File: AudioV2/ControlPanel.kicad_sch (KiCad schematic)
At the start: 39 parts, among them SW1 PWR SW, SW2 DEST sense (3PDT 3rd pole), U1 Pico 2 / RP2350, U2 PT2314-D, U5 BP5293-50 +5V

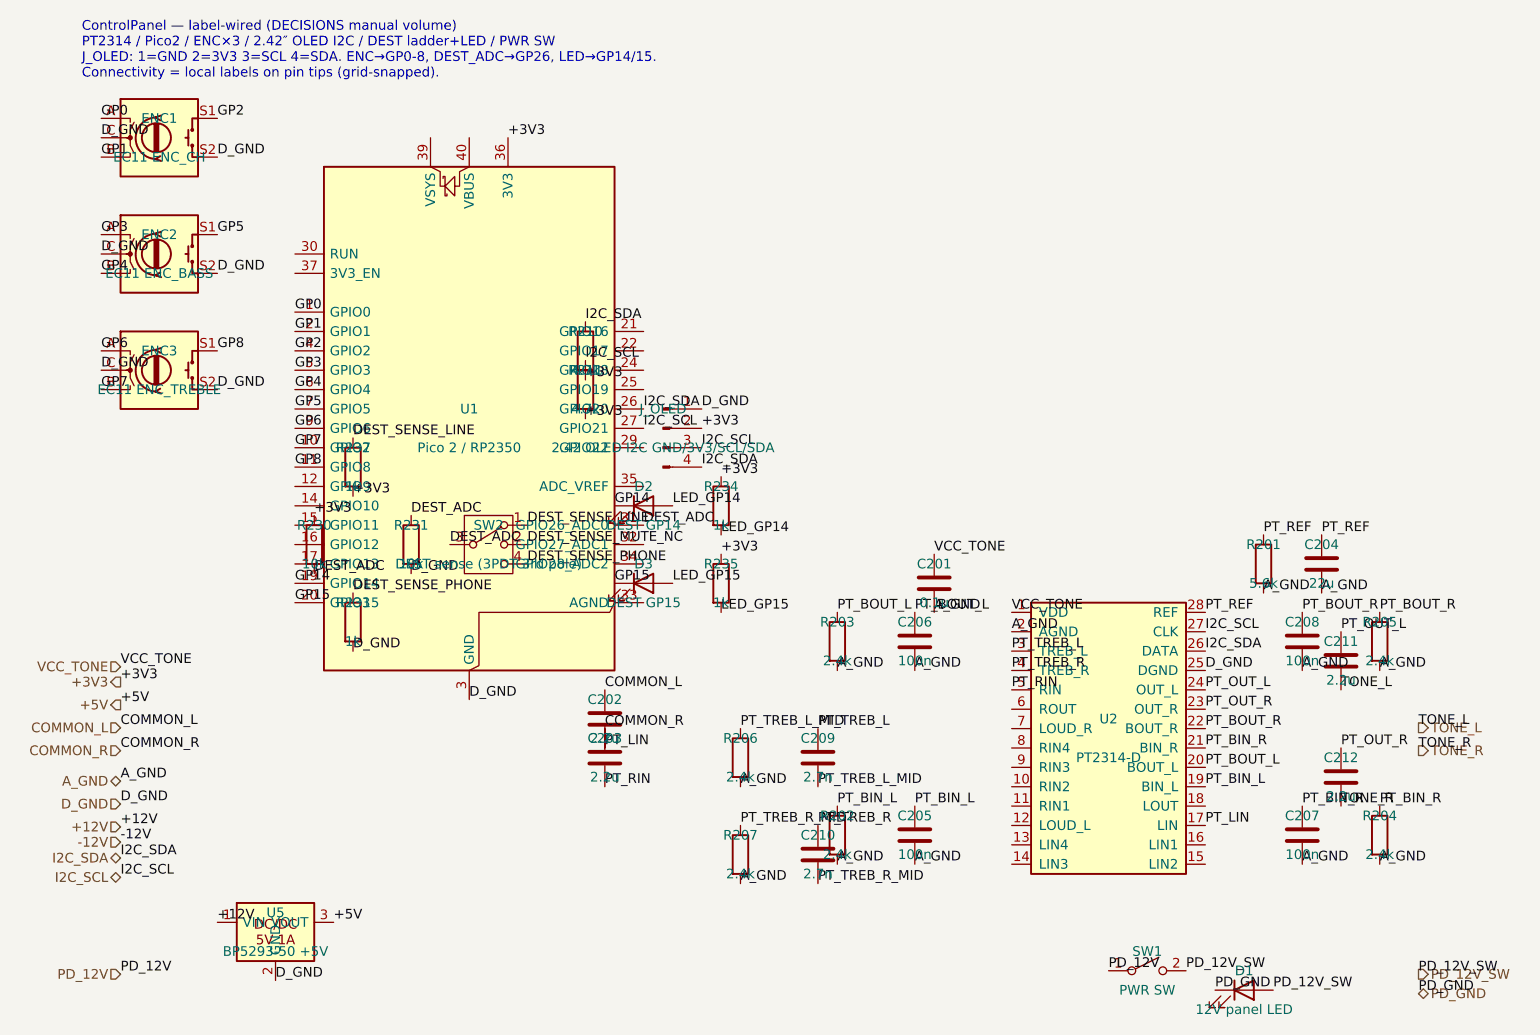
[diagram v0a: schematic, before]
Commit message: AudioV2: 全シートを再アノテーション、参照変更を生成スクリプトと文書へ反映
KiCad で再アノテーションし、参照の重複と未付番を解消（計58件が変更）。

- ControlPanel の C201-C208 が PowerModule と重複していたため 5xx 台へ移動
- 未付番だった J_OLED を J_OLED501 に
- RelayBoard で U301(MCP23017) と U302(ULN2803A SET側) が入れ替わり
  → MCP23017 は U302、SET側 ULN が U301。接続トポロジは変更なし
- OutputStage が 6xx 台へ、AmpModule の C7xx/R7xx が L/R 対称に整列
- これにより netlist 出力時の「注釈のエラー」警告が解消

wire_circuit_design.py は旧参照をハードコードしており、再生成すると
アノテーションが巻き戻る状態だった。生成関数の行範囲でスコープを切って
86箇所を同時置換（U1 が PowerModule と ControlPanel で別部品のため）。
サンドボックスで再生成して実図と突き合わせ、AmpModule / ControlPanel /
RelayBoard / AudioV2Case は参照・値とも完全一致することを確認。
変更前後どちらの生成物も ERC 80件で、本修正は ERC 中立。

文書側も 7ファイル52箇所を更新。PARTS.md の「R705-708」等の範囲表記は
振り直し後に連番でなくなるため書き直し、OutputStage の表は SW_SP3T×2 の
実ピン（ネット名で照合）に合わせた。DECISIONS.md の D1/D2/D3 は決定ID、
旧 Audio/ SW101 参照は別プロジェクト指定のため意図的に据え置き。

既知の未同期: PowerModule はスクリプトが一世代古い（USB-C+CH224 の PD
前段を生成するが実図は PD モジュール外付け）。参照対応が一意に決まらない
ため F1→F201 / U1→U201 / U3→U202 / J202→J201 のみ修正し、コンデンサ群は
未着手。OutputStage の J_RAIL601 も生成対象外。

ERC は実図 54件で変化なし。

Co-Authored-By: Claude Opus 5 <noreply@anthropic.com>
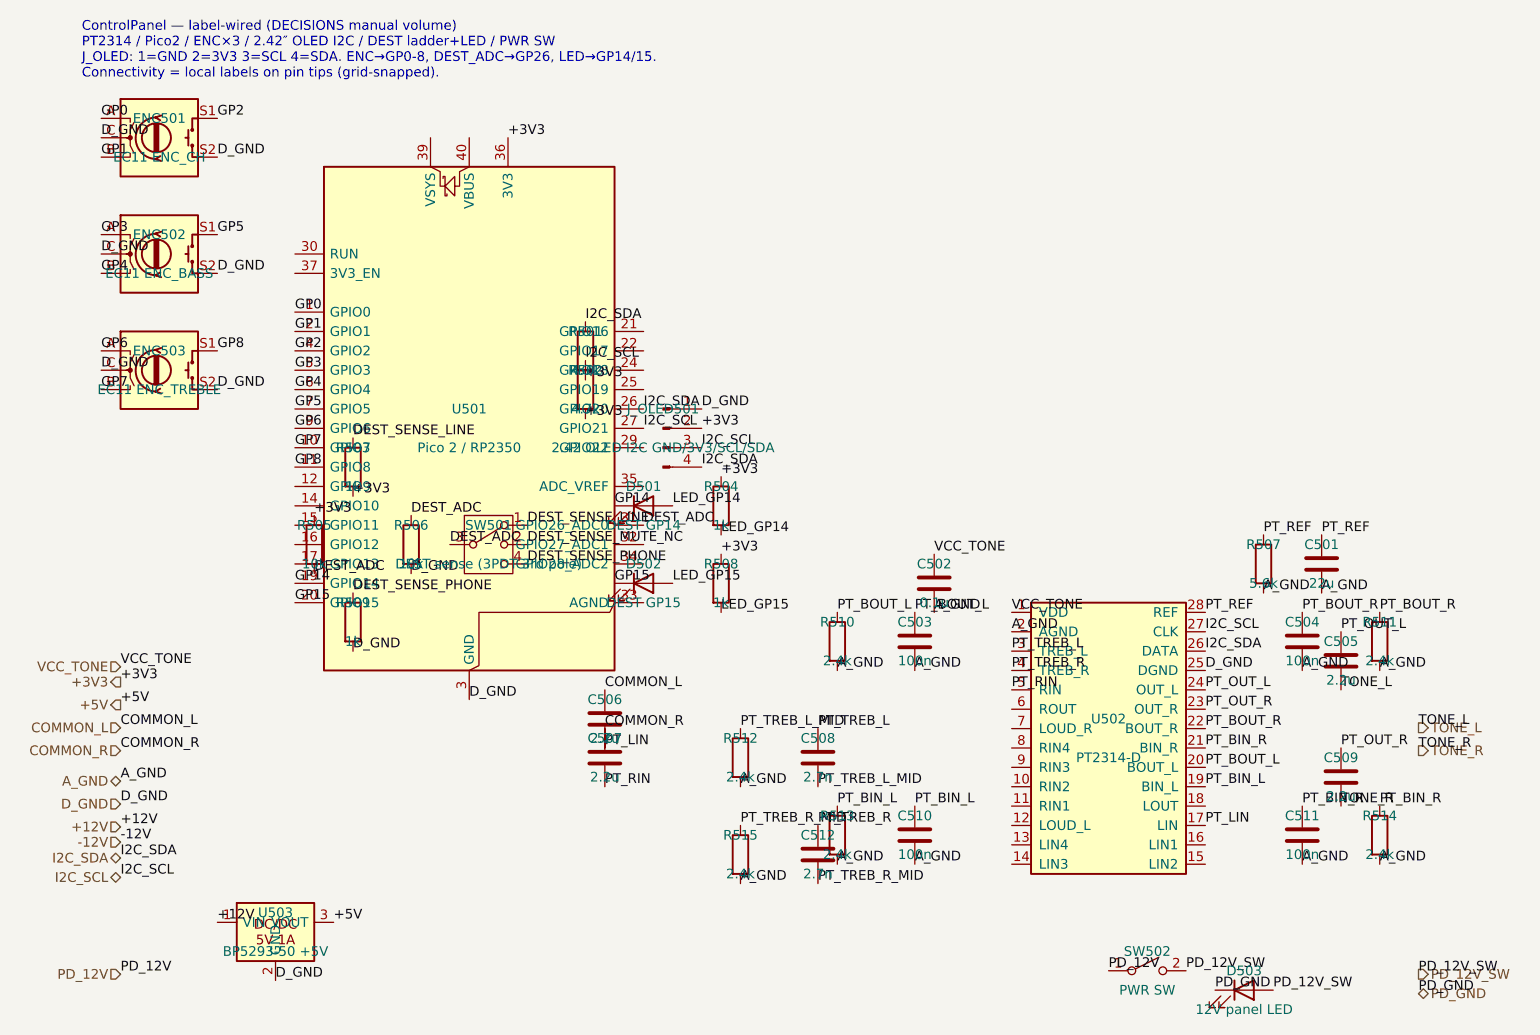
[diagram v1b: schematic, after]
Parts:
- renumbered C204 to C501, C201 to C502, C206 to C503, C208 to C504, C211 to C505, C202 to C506, C203 to C507, C209 to C508, C212 to C509, C205 to C510, C207 to C511, C210 to C512, D2 to D501, D3 to D502, D1 to D503, ENC1 to ENC501, ENC2 to ENC502, ENC3 to ENC503, J_OLED to J_OLED501, R210 to R501, R211 to R502, R232 to R503, R234 to R504, R230 to R505, R231 to R506, R201 to R507, R235 to R508, R233 to R509, R203 to R510, R205 to R511, R206 to R512, R202 to R513, R204 to R514, R207 to R515, SW2 to SW501, SW1 to SW502, U1 to U501, U2 to U502, U5 to U503

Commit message: AudioV2: RelayBoard/AmpModuleをAmpBank(10ch統合)へ置き換え、電源を+15V/-15Vへ改名
AGENT_HANDOFF.md §2.9の手順3〜5を実施。旧RelayBoard(5ch×2)+AmpModule(×10)を
削除し、TMUX7612切替・常時給電のAmpBank 1枚(AmpChannel×10)へ統合。親シートを
差し替え、+12V/-12Vネットを全シートで+15V/-15Vへ改名(PowerModuleの電源ICも
DKMW20F-12→DKMW20F-15へ実体差し替え)。

gen_parts_bom.pyの生成元をAmpBank.kicad_schへ切替、AGENT_HANDOFF/PARTS/
CIRCUIT_DESIGN/WIRINGの該当箇所を更新。ローカルWindows環境でのビルド/検証を
通すためkicad-run.shにPYTHONUTF8=1を追加。

Co-Authored-By: Claude Sonnet 5 <noreply@anthropic.com>
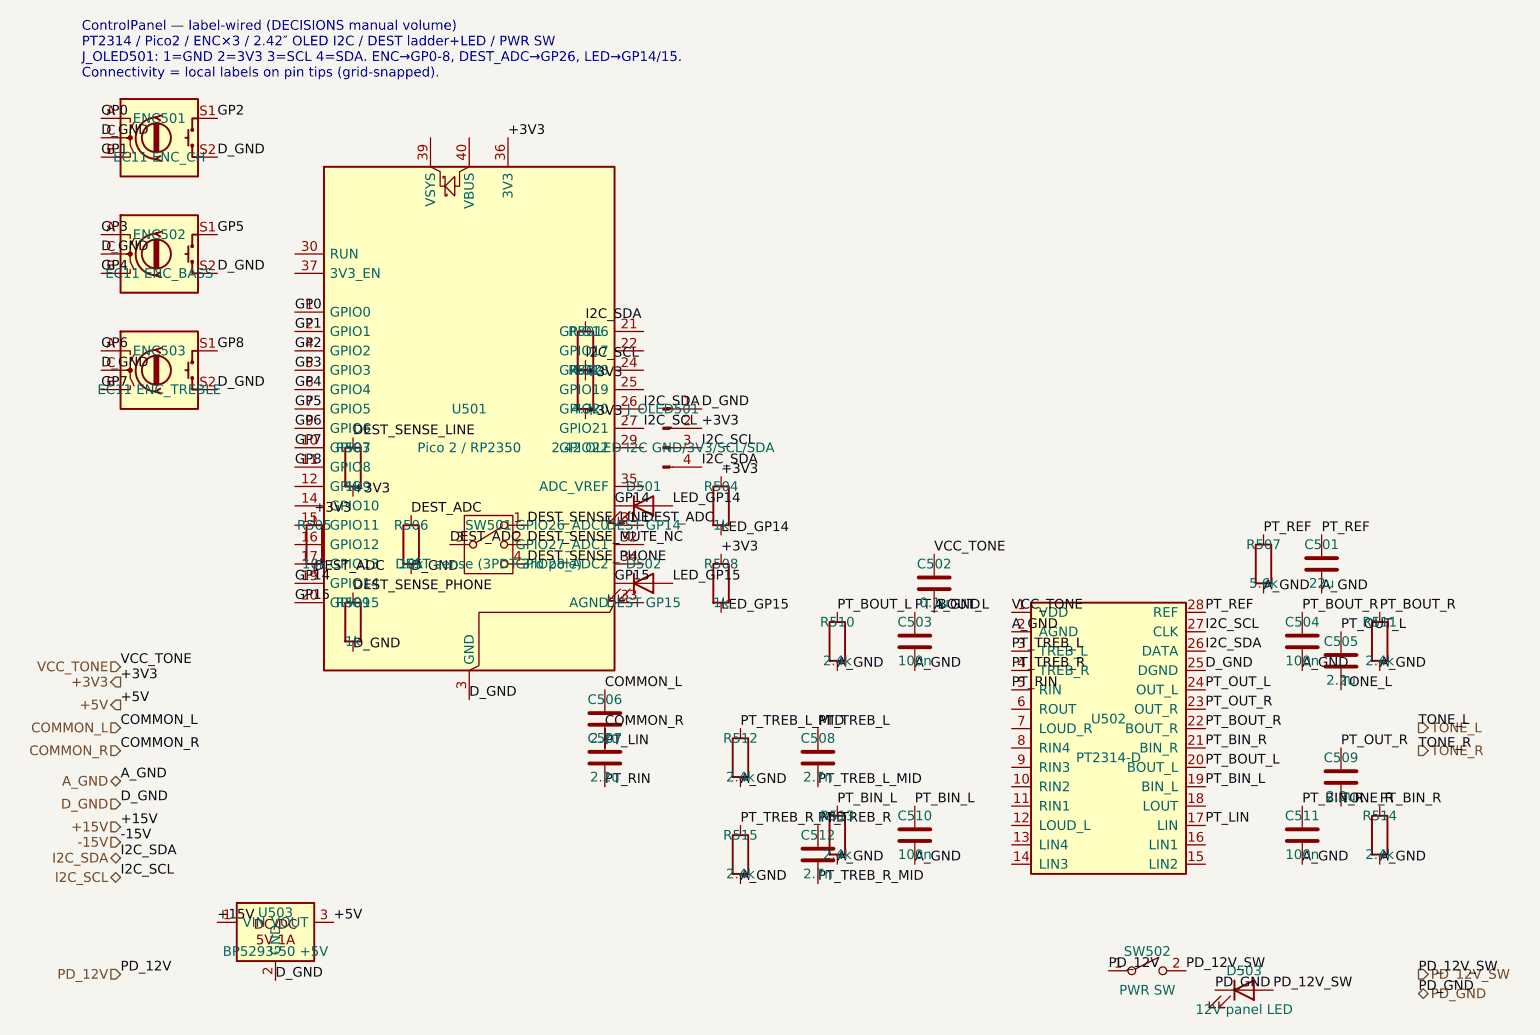
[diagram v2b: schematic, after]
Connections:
- net +12V renamed +15V
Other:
- note added: "ControlPanel — label-wired (DECISIONS manual volume) PT2314 / Pico2 / ENC×3 / 2.42″ OLED I2C / DEST ladder+LED / PWR SW J_OLED501: 1=GND 2=3V3 3=SCL 4=SDA. ENC→GP0-8, DEST_ADC→GP26, LED→GP14/15. Connectivity = local labels on pin tips (grid-snapped)."
- note removed: "ControlPanel — label-wired (DECISIONS manual volume) PT2314 / Pico2 / ENC×3 / 2.42″ OLED I2C / DEST ladder+LED / PWR SW J_OLED: 1=GND 2=3V3 3=SCL 4=SDA. ENC→GP0-8, DEST_ADC→GP26, LED→GP14/15. Connectivity = local labels on pin tips (grid-snapped)."
